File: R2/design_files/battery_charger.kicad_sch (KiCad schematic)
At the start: 18 parts, among them J6 Conn_01x02, U10 PUMH10,115, U11 BQ25622E

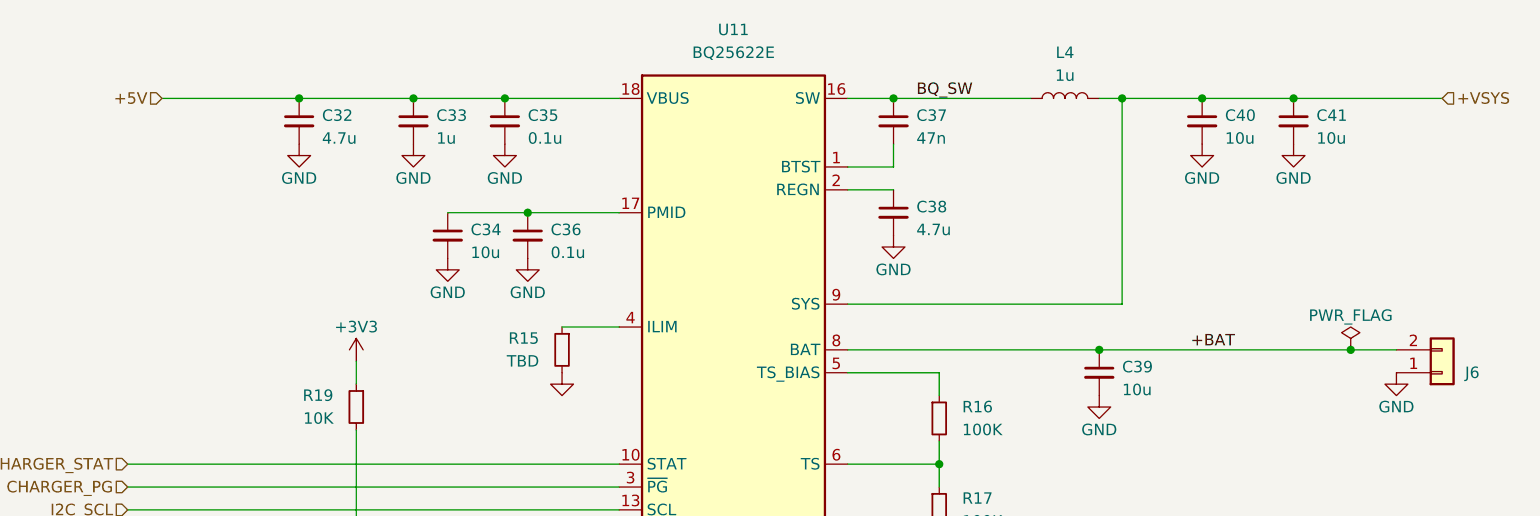
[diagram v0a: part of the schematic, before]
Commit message: Added test points
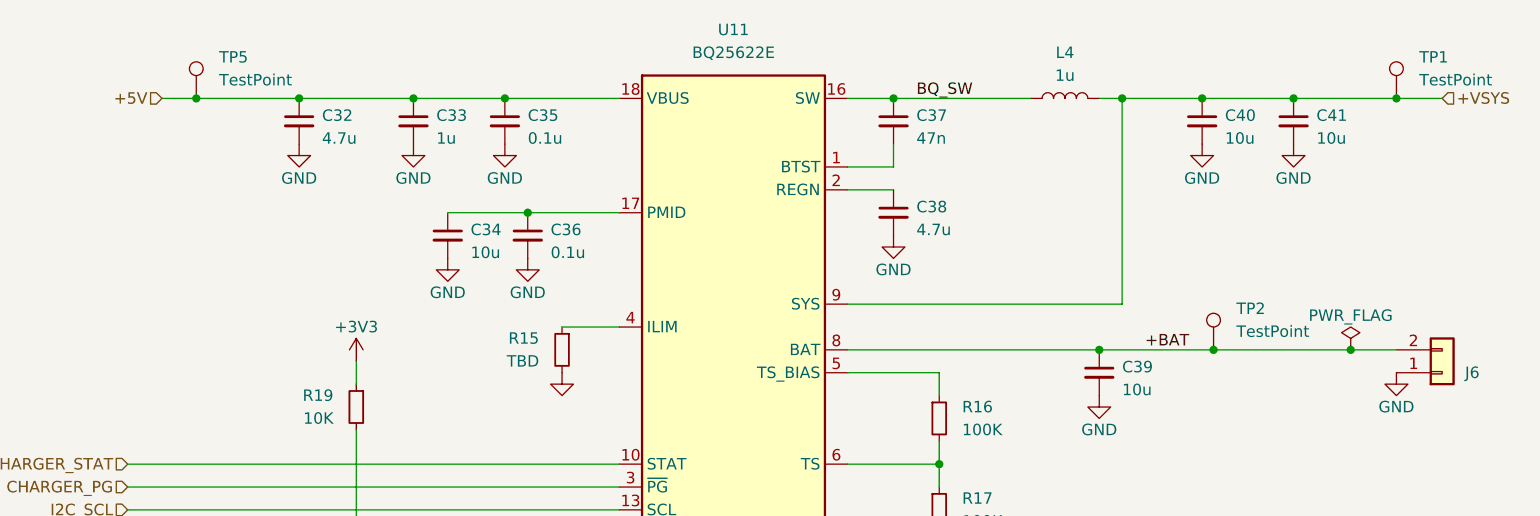
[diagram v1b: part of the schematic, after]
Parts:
- added TP1, TP2, TP5: TestPoint, TestPoint:TestPoint_Pad_D1.0mm, symbol Connector:TestPoint
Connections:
- net +5V: now also TP5.1
- net +BAT: now also TP2.1
- net +VSYS: now also TP1.1
